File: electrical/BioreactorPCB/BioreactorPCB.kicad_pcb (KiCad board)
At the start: 2 copper layers, 67 x 58.2 mm, 31 parts, among them IC1 AL5809-20P1-7, J1 61300311121, J2 61300311121, J3 OSTTC022162, J4 PJ-202A, J5 OSTTC022162, J6 OSTTC022162, J7 OSTTC042162, J8 OSTTC042162, J9 OSTTC042162, Q1 2N3905, Q2 IRF540N, Q3 FQP47P06, U1 OPT101P, U2 L293D, U3 LM329xZ

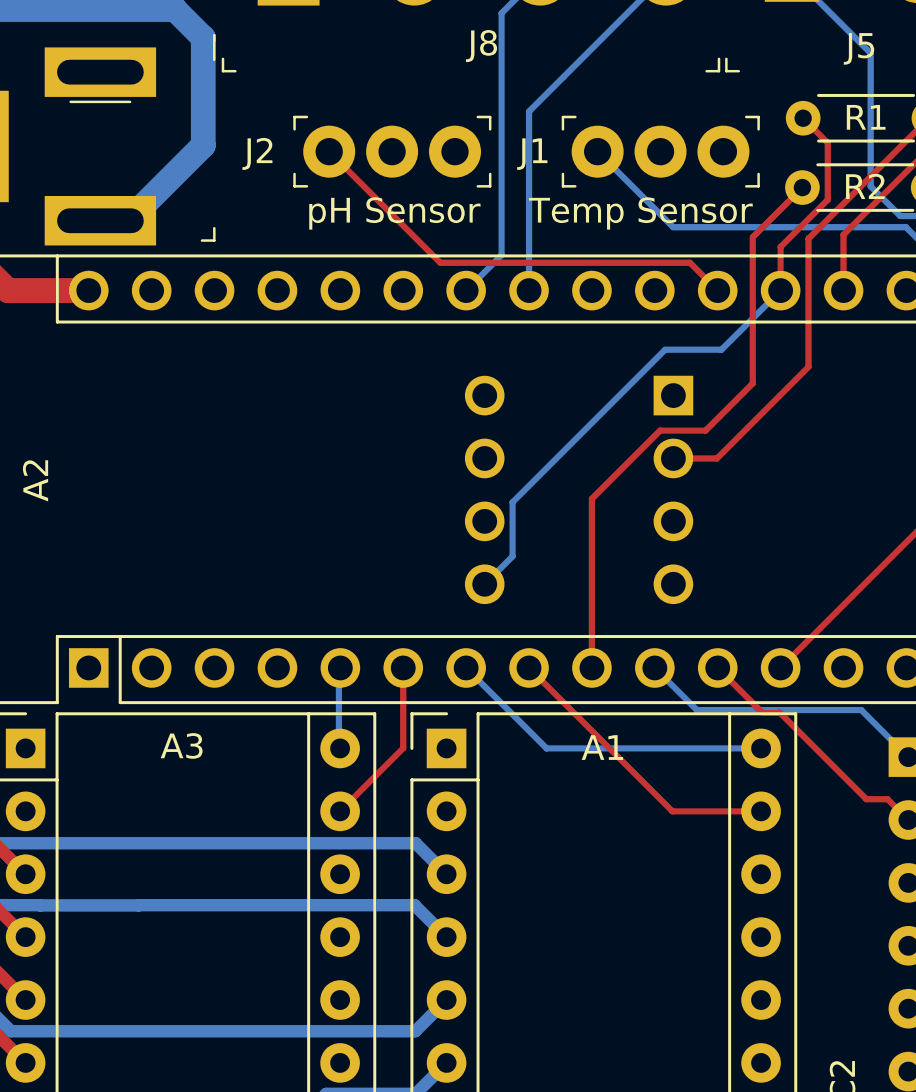
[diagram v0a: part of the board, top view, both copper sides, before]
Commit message: Arduino code is validated and working on Arduino Nano Every and board layout updated to match latest.
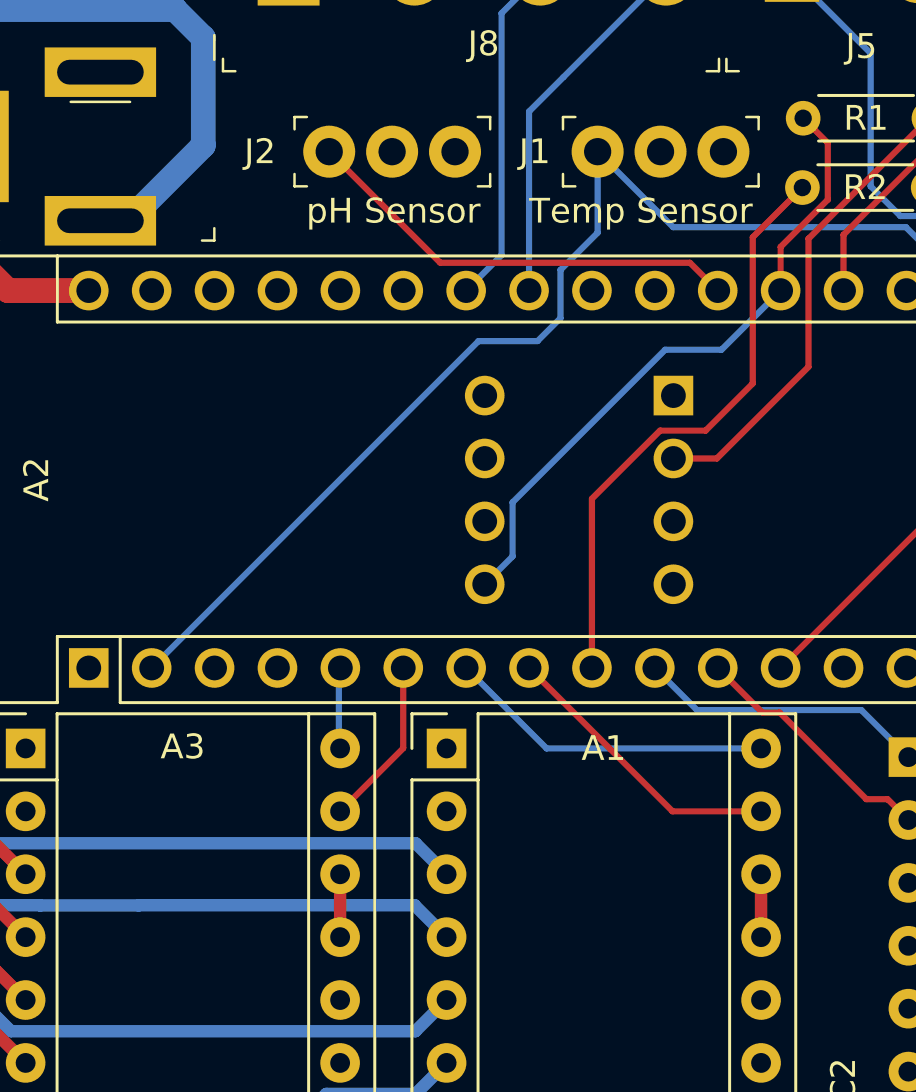
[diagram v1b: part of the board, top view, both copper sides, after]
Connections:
- A1 pad 14: Net-(A1-Pad14) -> Net-(A1-Pad13)
- A2 pad 16: TEMP_OUT -> Net-(A2-Pad16)
- A2 pad 2: Net-(A2-Pad2) -> TEMP_OUT
- A3 pad 14: Net-(A3-Pad14) -> Net-(A3-Pad13)
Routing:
- net TEMP_OUT: track 17.3 -> 47.0 mm
- net Net-(A3-Pad13): track 0.00 -> 2.54 mm
- net Net-(A1-Pad13): track 0.00 -> 2.54 mm

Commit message: PCB rev 2.0 development underway
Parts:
- removed G***: LOGO, Desktop:AGARALOGO
- removed R1: 1M, Resistor_THT:R_Axial_DIN0204_L3.6mm_D1.6mm_P5.08mm_Horizontal
- removed R4: 2.2K, Resistor_THT:R_Axial_DIN0204_L3.6mm_D1.6mm_P5.08mm_Horizontal
- removed R5: 10K, Resistor_THT:R_Axial_DIN0204_L3.6mm_D1.6mm_P5.08mm_Horizontal
- removed R6: 22K, Resistor_THT:R_Axial_DIN0204_L3.6mm_D1.6mm_P5.08mm_Horizontal
- removed REF** (x2): MountingHole_3.2mm_M3_DIN965_Pad, MountingHole:MountingHole_3.2mm_M3_DIN965_Pad
- removed REF**: OSHW-Logo2_7.3x6mm_SilkScreen, Symbol:OSHW-Logo2_7.3x6mm_SilkScreen
- removed U1: OPT101P, digikey-footprints:DIP-8_W7.62mm
- removed U3: LM329xZ, Package_TO_SOT_THT:TO-92_Inline
- added D1: LED, LED_THT:LED_D5.0mm_Horizontal_O3.81mm_Z9.0mm, F.Cu at (122.7, 40.6)
- added H1: MountingHole_Pad, MountingHole:MountingHole_3.2mm_M3_DIN965_Pad, F.Cu at (69.7, 57.5)
- added H2: MountingHole_Pad, MountingHole:MountingHole_3.2mm_M3_DIN965_Pad, F.Cu at (69.7, 112.5)
- added H3: MountingHole_Pad, MountingHole:MountingHole_3.2mm_M3_DIN965_Pad, F.Cu at (119.7, 112.5)
- added H4: MountingHole_Pad, MountingHole:MountingHole_3.2mm_M3_DIN965_Pad, F.Cu at (141.8, 91.9)
- added H5: MountingHole_Pad, MountingHole:MountingHole_3.2mm_M3_DIN965_Pad, F.Cu at (102.7, 34.7)
- added H6: MountingHole_Pad, MountingHole:MountingHole_3.2mm_M3_DIN965_Pad, F.Cu at (102.7, 49.2)
- added H7: MountingHole_Pad, MountingHole:MountingHole_3.2mm_M3_DIN965_Pad, F.Cu at (121.2, 34.7)
- added H8: MountingHole_Pad, MountingHole:MountingHole_3.2mm_M3_DIN965_Pad, F.Cu at (121.2, 49.2)
- added IC2: VEML7700-TR, VEML7700-TR:VEML7700, F.Cu at (101.2, 38.6)
- added J10: 171856-0006, 171856-0006:HDRV6W99P0X254_1X6_1509X635X1100P, B.Cu at (95.7, 35.8)
- added S1: GW12RCH, GW12RCH:GW12RCH, F.Cu at (86.6, 46.2)
- J3: value OSTTC022162 -> 171856-0006; footprint digikey-footprints:Term_Block_1x2_P5.08MM -> 171856-0006:HDRV6W99P0X254_1X6_1509X635X1100P
- moved J6 50.8 mm to (112.5, 111.1)
- moved J5 50.8 mm to (96.7, 111.1)
- moved J3 44.3 mm to (96.7, 77.7), turned to 0 degrees
- moved J2 42.1 mm to (117.0, 101.2), turned to 90 degrees
- moved J8 41.6 mm to (118.0, 90.8), turned to 90 degrees
- moved J1 38.0 mm to (120.8, 101.2), turned to 90 degrees
- moved Q2 30.6 mm to (104.2, 91.8), turned to 0 degrees
- moved R3 28.7 mm to (99.0, 88.1), turned to 90 degrees
- moved C1 28.7 mm to (95.5, 92.2), turned to 0 degrees
- moved R2 25.2 mm to (96.3, 88.1), turned to 90 degrees
- moved Q1 23.5 mm to (104.5, 86.0), turned to 90 degrees
- moved IC1 21.6 mm to (110.0, 84.7), turned to 270 degrees
- moved Q3 21.5 mm to (86.9, 50.2), turned to 180 degrees
- moved J4 20.8 mm to (73.2, 49.2)
- moved U2 20.2 mm to (95.5, 102.8), turned to 90 degrees
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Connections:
- A1 pad 10: Net-(A1-Pad10) -> (no net)
- A1 pad 11: Net-(A1-Pad11) -> (no net)
- A1 pad 12: Net-(A1-Pad12) -> (no net)
- A1 pad 9: Net-(A1-Pad9) -> (no net)
- A2 pad 1: Net-(A2-Pad1) -> (no net)
- A2 pad 13: Net-(A2-Pad13) -> (no net)
- A2 pad 14: Net-(A2-Pad14) -> (no net)
- A2 pad 15: Net-(A2-Pad15) -> (no net)
- A2 pad 16: Net-(A2-Pad16) -> (no net)
- A2 pad 17: Net-(A2-Pad17) -> +3V3
- A2 pad 18: Net-(A2-Pad18) -> (no net)
- A2 pad 19: PHOTO_OUT -> (no net)
- A2 pad 21: Net-(A2-Pad21) -> (no net)
- A2 pad 22: Net-(A2-Pad22) -> (no net)
- A2 pad 23: Net-(A2-Pad23) -> SDA
- A2 pad 24: Net-(A2-Pad24) -> SCL
- A2 pad 25: Net-(A2-Pad25) -> (no net)
- A2 pad 26: Net-(A2-Pad26) -> (no net)
- A2 pad 28: Net-(A2-Pad28) -> (no net)
- A2 pad 3: Net-(A2-Pad3) -> (no net)
- A3 pad 10: Net-(A3-Pad10) -> (no net)
- A3 pad 11: Net-(A3-Pad11) -> (no net)
- A3 pad 12: Net-(A3-Pad12) -> (no net)
- A3 pad 9: Net-(A3-Pad9) -> (no net)
- J3 pad 1: GND -> Net-(IC1-Pad2)
- J3 pad 2: Net-(IC1-Pad2) -> GND
- J8 pad 3: Net-(A2-Pad24) -> SCL
- J8 pad 4: Net-(A2-Pad23) -> SDA
- Q3 pad 2: Net-(J4-Pad1) -> Net-(Q3-Pad2)
- U2 pad 10: Net-(U2-Pad10) -> (no net)
- U2 pad 11: Net-(U2-Pad11) -> (no net)
- U2 pad 14: Net-(U2-Pad14) -> (no net)
- U2 pad 15: Net-(U2-Pad15) -> (no net)
- U2 pad 9: Net-(U2-Pad9) -> (no net)
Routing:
- net +12V: track 164.8 -> 115.9 mm
- net SCL: track 0.00 -> 43.1 mm
- net PH_OUT: track 18.0 -> 56.1 mm
- net SDA: track 0.00 -> 35.0 mm
- net Net-(J5-Pad1): track 52.2 -> 18.7 mm
- net Net-(J5-Pad2): track 40.7 -> 8.76 mm
- net Net-(A2-Pad10): track 11.7 -> 42.1 mm
- net Net-(A2-Pad11): track 10.2 -> 36.8 mm
- net PHOTO_OUT: track 26.5 -> 0.00 mm
- net +3V3: track 0.00 -> 25.1 mm
- net Net-(A1-Pad15): track 11.8 -> 31.9 mm
- net Net-(R1-Pad2): track 19.0 -> 0.00 mm
- net Net-(Q1-Pad2): track 26.5 -> 9.50 mm
- net Net-(A1-Pad6): track 26.8 -> 10.5 mm
- net Net-(R4-Pad1): track 15.5 -> 0.00 mm
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- added copper zone on B.Cu, net +5V
- added copper zone on F.Cu, net GND
- added copper zone on B.Cu, net GND2
- removed copper zone on F.Cu, net +5V
- removed copper zone on B.Cu, net GND
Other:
- board size 67 x 58.2 mm -> 56.1 x 78.1 mm
- board text added: "Temp"
- board text added: "pH"
- board text removed: "LED"
- board text removed: "Temp Sensor"
- board text removed: "pH Sensor"

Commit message: Completed rev 2.0 schematic for real now
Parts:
- removed A3: Pololu_Breakout_A4988, Module:Pololu_Breakout-16_15.2x20.3mm
- added C3: .1 uF, Capacitor_THT:CP_Radial_Tantal_D5.0mm_P2.50mm, F.Cu at (160.3, 114.0)
- added C4: 22 pf, Capacitor_THT:CP_Radial_Tantal_D4.5mm_P2.50mm, F.Cu at (137.9, 83.6)
- added C5: 22 pf, Capacitor_THT:CP_Radial_Tantal_D4.5mm_P2.50mm, F.Cu at (144.0, 83.6)
- added C6: .1 uF, Capacitor_THT:CP_Radial_Tantal_D5.0mm_P2.50mm, F.Cu at (131.5, 80.5)
- added C7: .1 uF, Capacitor_THT:CP_Radial_Tantal_D5.0mm_P2.50mm, F.Cu at (139.5, 77.3)
- added C8: 100 uF, Capacitor_THT:CP_Radial_D5.0mm_P2.50mm, F.Cu at (199.6, 65.3)
- added C9: 330 uF, Capacitor_THT:CP_Radial_D5.0mm_P2.50mm, F.Cu at (199.6, 58.7)
- added D2: LED, LED_THT:LED_D5.0mm, F.Cu at (171.4, 94.4)
- added D3: LED, LED_THT:LED_D5.0mm_Horizontal_O3.81mm_Z9.0mm, F.Cu at (200.8, 99.3)
- added D4: 1N5819, Diode_THT:D_DO-41_SOD81_P10.16mm_Horizontal, F.Cu at (154.9, 82.8)
- added H10: MountingHole_Pad, MountingHole:MountingHole_3.2mm_M3_DIN965_Pad, F.Cu at (177.5, 132.5)
- added H11: MountingHole_Pad, MountingHole:MountingHole_3.2mm_M3_DIN965_Pad, F.Cu at (184.2, 124.7)
- added H12: MountingHole_Pad, MountingHole:MountingHole_3.2mm_M3_DIN965_Pad, F.Cu at (184.6, 131.8)
- added H9: MountingHole_Pad, MountingHole:MountingHole_3.2mm_M3_DIN965_Pad, F.Cu at (169.4, 138.8)
- added J11: Conn_01x06_Male, Connector_Molex:Molex_KK-254_AE-6410-06A_1x06_P2.54mm_Vertical, F.Cu at (200.7, 93.7)
- added J12: Conn_02x03_Odd_Even, Connector_PinHeader_2.54mm:PinHeader_2x03_P2.54mm_Vertical, F.Cu at (112.9, 81.4)
- added J13: PJ-202A, digikey-footprints:Barrel_Jack_5.5mmODx2.1mmID_PJ-202A, F.Cu at (182.6, 67.0)
- added J14: Conn_01x05_Male, Connector_Molex:Molex_KK-254_AE-6410-05A_1x05_P2.54mm_Vertical, F.Cu at (168.2, 125.0)
- added L1: 330 uH, Inductor_THT:L_Radial_D12.0mm_P6.00mm_MuRATA_1900R, F.Cu at (179.9, 78.5)
- added Q4: TL2575HV-05IKV, Package_TO_SOT_THT:TO-220-5_P3.4x3.8mm_StaggerEven_Lead7.13mm_TabDown, F.Cu at (155.4, 75.2)
- added R1: 330, Resistor_THT:R_Axial_DIN0204_L3.6mm_D1.6mm_P5.08mm_Horizontal, F.Cu at (170.4, 109.3)
- added R10: 10K, Resistor_THT:R_Axial_DIN0204_L3.6mm_D1.6mm_P5.08mm_Horizontal, F.Cu at (167.3, 130.5)
- added R11: 10K, Resistor_THT:R_Axial_DIN0204_L3.6mm_D1.6mm_P5.08mm_Horizontal, F.Cu at (167.3, 133.7)
- added R4: 330, Resistor_THT:R_Axial_DIN0204_L3.6mm_D1.6mm_P5.08mm_Horizontal, F.Cu at (151.6, 112.3)
- added R5: 1K, Resistor_THT:R_Axial_DIN0204_L3.6mm_D1.6mm_P5.08mm_Horizontal, F.Cu at (124.4, 64.9)
- added R6: 1K, Resistor_THT:R_Axial_DIN0204_L3.6mm_D1.6mm_P5.08mm_Horizontal, F.Cu at (123.7, 69.0)
- added R7: 10K, Resistor_THT:R_Axial_DIN0204_L3.6mm_D1.6mm_P5.08mm_Horizontal, F.Cu at (102.3, 75.6)
- added R8: 200K, Resistor_THT:R_Axial_DIN0207_L6.3mm_D2.5mm_P10.16mm_Horizontal, F.Cu at (217.2, 91.7)
- added R9: 10K, Resistor_THT:R_Axial_DIN0204_L3.6mm_D1.6mm_P5.08mm_Horizontal, F.Cu at (151.6, 140.7)
- added S2: PEC11R-4215F-S0024, digikey-footprints:Rotary_Encoder_Switched_PEC11R, F.Cu at (152.3, 129.9)
- added U1: L293D, Package_DIP:DIP-16_W7.62mm, F.Cu at (90.9, 94.7)
- added U3: ATMEGA328P-AUR, digikey-footprints:TQFP-32_7x7mm, F.Cu at (138.6, 61.2)
- added U4: TCA39306DCUR, TCA39306DCUR:TCA39306DCUR, F.Cu at (226.2, 95.3)
- added Y1: 16 mHz, Crystal:Crystal_HC49-U_Vertical, F.Cu at (104.8, 66.6)
- A2: value Arduino_Nano_v3.x -> Pololu_Breakout_A4988; footprint Module:Arduino_Nano -> Module:Pololu_Breakout-16_15.2x20.3mm
- C1, C2: footprint Capacitor_THT:.1in_pitch -> Capacitor_THT:CP_Radial_Tantal_D5.0mm_P2.50mm
- D1: footprint LED_THT:LED_D5.0mm_Horizontal_O3.81mm_Z9.0mm -> LED_THT:LED_D5.0mm
- J10: value 171856-0006 -> USB_B; footprint 171856-0006:HDRV6W99P0X254_1X6_1509X635X1100P -> Connector_USB:USB_B_Lumberg_2411_02_Horizontal; moved to F.Cu
- J3: value 171856-0006 -> Conn_01x05_Male; footprint 171856-0006:HDRV6W99P0X254_1X6_1509X635X1100P -> Connector_Molex:Molex_KK-254_AE-6410-05A_1x05_P2.54mm_Vertical
- J4: value PJ-202A -> Conn_01x06_Male; footprint digikey-footprints:Barrel_Jack_5.5mmODx2.1mmID_PJ-202A -> Connector_Molex:Molex_KK-254_AE-6410-06A_1x06_P2.54mm_Vertical
- Q2: footprint Package_TO_SOT_THT:TO-220-3_Vertical -> Package_TO_SOT_THT:TO-220-3_Horizontal_TabDown
- Q3: footprint FQP47P06:TO254P1067X483X2286-3 -> Package_TO_SOT_THT:TO-220-3_Horizontal_TabDown
- U2: value L293D -> FT232RL; footprint Package_DIP:DIP-16_W7.62mm -> Package_SO:SSOP-28_5.3x10.2mm_P0.65mm
- moved H6 137.1 mm to (232.5, 93.3)
- moved H5 134.6 mm to (217.8, 104.5)
- moved IC2 122.9 mm to (206.9, 101.4), turned to 0 degrees
- moved H7 116.3 mm to (219.2, 97.3)
- moved H8 105.3 mm to (209.4, 106.6)
- moved S1 104.1 mm to (190.2, 57.0), turned to 0 degrees
- moved U2 93.7 mm to (189.2, 98.7), turned to 0 degrees
- moved J10 86.2 mm to (152.7, 100.4), turned to 0 degrees
- moved Q3 84.8 mm to (167.8, 75.7), turned to 0 degrees
- moved D1 77.8 mm to (178.9, 94.4), turned to 0 degrees
- moved H2 75.0 mm to (133.8, 73.6)
- moved H1 59.5 mm to (125.8, 77.2)
- moved J9 56.9 mm to (113.8, 119.1), turned to 0 degrees
- moved H3 47.5 mm to (141.9, 70.5)
- moved IC1 46.2 mm to (147.1, 57.1), turned to 0 degrees
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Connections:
- A1 pad 15: Net-(A1-Pad15) -> D5
- A1 pad 16: Net-(A1-Pad16) -> D4
- A2 pad 1: (no net) -> GND
- A2 pad 10: Net-(A2-Pad10) -> (no net)
- A2 pad 11: Net-(A2-Pad11) -> (no net)
- A2 pad 12: Net-(A2-Pad12) -> (no net)
- A2 pad 13: (no net) -> Net-(A2-Pad13)
- A2 pad 14: (no net) -> Net-(A2-Pad13)
- A2 pad 15: (no net) -> D3
- A2 pad 16: (no net) -> D2
- A2 pad 2: TEMP_OUT -> +5V
- A2 pad 3: (no net) -> Net-(A2-Pad3)
- A2 pad 4: GND -> Net-(A2-Pad4)
- A2 pad 7: Net-(A1-Pad16) -> GND
- A2 pad 8: Net-(A1-Pad15) -> +12V
- A2 pad 9: Net-(A2-Pad9) -> (no net)
- D1 pad 1: GND2 -> Net-(D1-Pad1)
- D1 pad 2: Net-(D1-Pad2) -> +5V
- IC2 pad 1: Net-(IC2-Pad1) -> SCL1
- IC2 pad 2: Net-(IC2-Pad2) -> 3V3_2
- IC2 pad 4: Net-(IC2-Pad4) -> SDA1
- J10 pad 1: Net-(D1-Pad2) -> (no net)
- J10 pad 2: GND2 -> Net-(J10-Pad2)
- J10 pad 3: GND2 -> Net-(J10-Pad3)
- J10 pad 4: Net-(IC2-Pad1) -> GND
- J10 pad 5: Net-(IC2-Pad2) -> GND
- J3 pad 1: Net-(IC1-Pad2) -> BUTTON
- J3 pad 2: GND -> ROT_A
- J3 pad 3: GND -> ROT_B
- J3 pad 4: SCL -> GND
- J3 pad 5: +3V3 -> +5V
- J4 pad 1: Net-(J4-Pad1) -> +3V3
- J4 pad 2: GND -> SDA
- J4 pad 3: GND -> SCL
- J9 pad 1: Net-(A3-Pad6) -> Net-(A2-Pad6)
- J9 pad 2: Net-(A3-Pad5) -> Net-(A2-Pad5)
- J9 pad 3: Net-(A3-Pad4) -> Net-(A2-Pad4)
- J9 pad 4: Net-(A3-Pad3) -> Net-(A2-Pad3)
- R2 pad 2: Net-(A2-Pad9) -> D6
- R3 pad 2: Net-(A2-Pad12) -> D9
- S1 pad 5: Net-(J4-Pad1) -> Net-(J13-Pad1)
- U2 pad 1: Net-(A2-Pad10) -> RX
- U2 pad 12: GND -> (no net)
- U2 pad 13: GND -> (no net)
- U2 pad 15: (no net) -> Net-(J10-Pad3)
- U2 pad 16: +5V -> Net-(J10-Pad2)
- U2 pad 2: Net-(A2-Pad11) -> Net-(C3-Pad2)
- U2 pad 3: Net-(J5-Pad2) -> (no net)
- U2 pad 4: GND -> +5V
- U2 pad 5: GND -> TX
- U2 pad 6: Net-(J5-Pad1) -> (no net)
- U2 pad 8: +12V -> (no net)
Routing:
- net +12V: track 115.9 -> 0.00 mm
- net PH_OUT: track 56.1 -> 0.00 mm
- net TEMP_OUT: track 53.0 -> 0.00 mm
- net SCL: track 43.1 -> 0.00 mm
- net Net-(A2-Pad10): track 42.1 -> 0.00 mm
- net Net-(A2-Pad11): track 36.8 -> 0.00 mm
- net SDA: track 35.0 -> 0.00 mm
- net Net-(A1-Pad15): track 31.9 -> 0.00 mm
- net Net-(A1-Pad16): track 27.4 -> 0.00 mm
- net +3V3: track 25.1 -> 0.00 mm
- net Net-(J6-Pad1): track 23.3 -> 0.00 mm
- net Net-(J5-Pad1): track 18.7 -> 0.00 mm
- net Net-(A1-Pad3): track 18.1 -> 0.00 mm
- net Net-(A2-Pad12): track 17.4 -> 0.00 mm
- net Net-(A3-Pad3): track 17.1 -> 0.00 mm
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- removed copper zone on B.Cu, net +5V
- removed copper zone on F.Cu, net GND
- removed copper zone on B.Cu, net GND2
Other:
- board outline removed
- board text removed: "+"
- board text removed: "-"
- board text removed: "1A"
- board text removed: "1B"
- board text removed: "2A"
- board text removed: "2B"
- board text removed: "5V"
- board text removed: "CLK"
- board text removed: "DAT"
- board text removed: "GND"
- board text removed: "LCD"
- board text removed: "Microbial Bioreactor by Open Bioeconomy Lab - Agara remix"
- board text removed: "Temp"
- board text removed: "design by Sreenivas Eadara"
- board text removed: "heatmat"
- board text removed: "motor 1"
- board text removed: "motor 2"
- board text removed: "pH"
- board text removed: "stir motor"

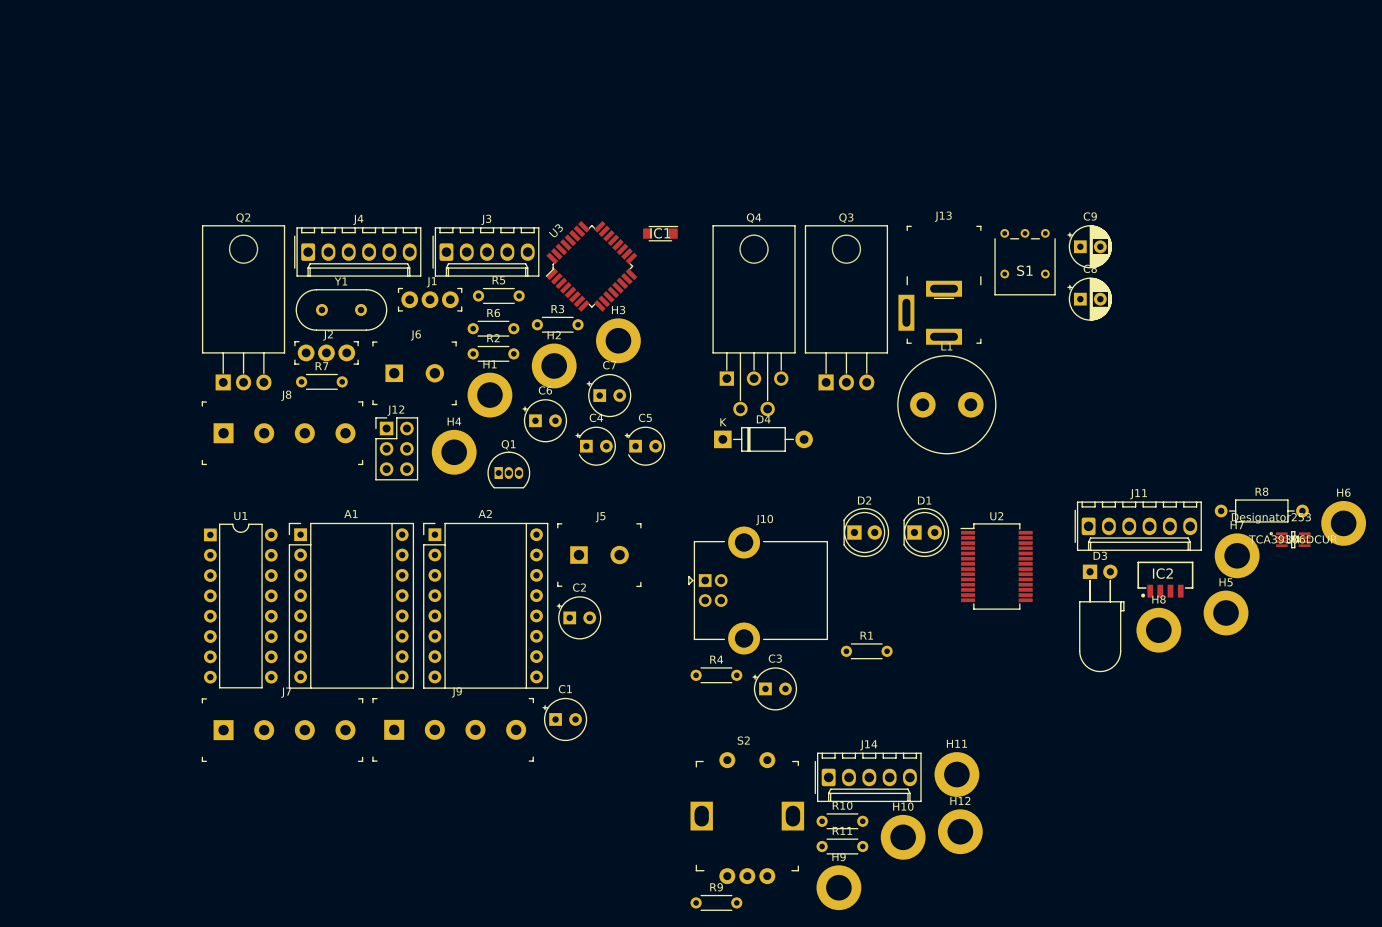
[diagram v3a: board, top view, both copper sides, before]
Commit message: added missing electrolytic capacitors for A4988 breakouts. Preliminary layout now in place
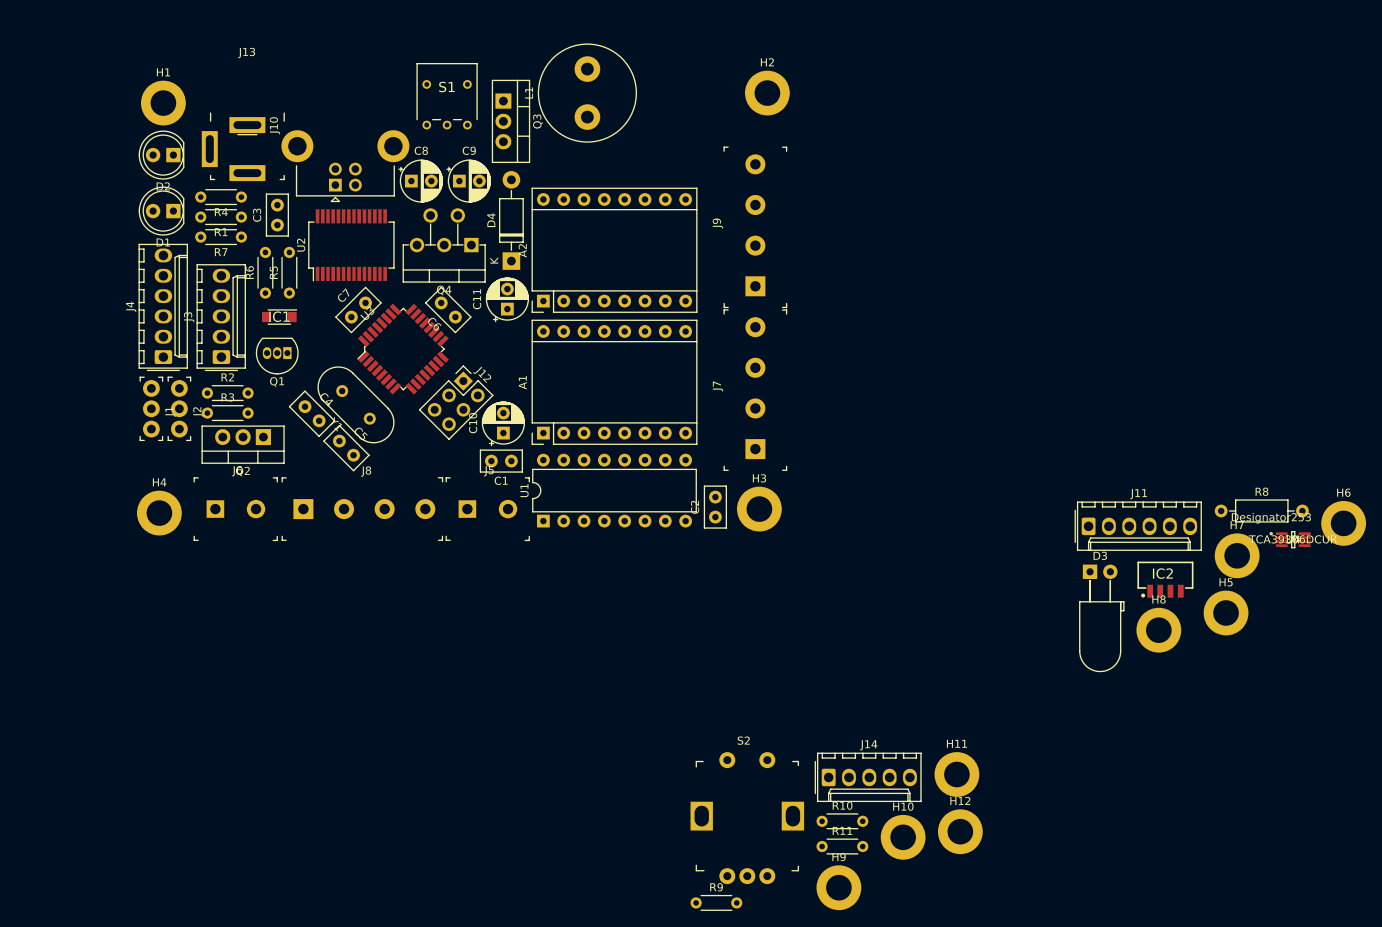
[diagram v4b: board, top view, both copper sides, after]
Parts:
- added C10: 100 uF, Capacitor_THT:CP_Radial_D5.0mm_P2.50mm, F.Cu at (127.5, 82.0)
- added C11: 100 uF, Capacitor_THT:CP_Radial_D5.0mm_P2.50mm, F.Cu at (128.0, 66.5)
- C1, C2, C3, C6, C7: footprint Capacitor_THT:CP_Radial_Tantal_D5.0mm_P2.50mm -> Capacitor_THT:C_Disc_D5.0mm_W2.5mm_P2.50mm
- C4, C5: footprint Capacitor_THT:CP_Radial_Tantal_D4.5mm_P2.50mm -> Capacitor_THT:C_Disc_D5.0mm_W2.5mm_P2.50mm
- Q2, Q3: footprint Package_TO_SOT_THT:TO-220-3_Horizontal_TabDown -> Package_TO_SOT_THT:TO-220-3_Vertical
- Q4: footprint Package_TO_SOT_THT:TO-220-5_P3.4x3.8mm_StaggerEven_Lead7.13mm_TabDown -> Package_TO_SOT_THT:TO-220-5_P3.4x3.7mm_StaggerEven_Lead3.8mm_Vertical
- moved D1 101.0 mm to (86.2, 54.2), turned to 180 degrees
- moved D2 97.3 mm to (86.2, 47.2), turned to 180 degrees
- moved R1 93.1 mm to (94.8, 55.0), turned to 180 degrees
- moved U2 90.1 mm to (108.5, 58.5), turned to 90 degrees
- moved J13 89.5 mm to (95.5, 46.5)
- moved C8 84.9 mm to (116.0, 50.5)
- moved C3 84.2 mm to (99.2, 56.0), turned to 90 degrees
- moved R4 82.5 mm to (94.8, 52.5), turned to 180 degrees
- moved C9 78.1 mm to (122.0, 50.5)
- moved J7 75.2 mm to (159.0, 84.0), turned to 90 degrees
- moved J9 71.5 mm to (159.0, 63.6), turned to 90 degrees
- moved S1 68.5 mm to (123.0, 43.5), turned to 180 degrees
- moved J10 67.7 mm to (106.5, 51.0), turned to 90 degrees
- moved L1 55.2 mm to (138.0, 42.5), turned to 90 degrees
- moved H1 54.8 mm to (85.0, 40.8)
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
